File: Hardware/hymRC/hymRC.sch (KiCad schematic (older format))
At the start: 42 parts, among them U1 KT8870, U2 MCP23017_SP, Y1 3.5795M

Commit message: huda calisma
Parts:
- added R13: 1K, symbol Device:R
- added U4: OptoCoupler, Package_DIP:SMDIP-4_W9.53mm_Clearance8mm, symbol Isolator:SFH617A-1X007T
- added U5: LM358, symbol Amplifier_Operational:LM358
- added U6: 4001, Package_DIP:DIP-24_W16.51mm_SMDSocket_LongPads, symbol 4xxx:4001
- gave numbers to parts that had none: 33
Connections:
- wire segments 152 -> 158
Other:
- note added: "- SQELCH BILGISI Optocoupler'dan gecirilecek\n- DTMF girisi icin LM358 kullanilacak (huda)\n- Mors vb baglantisi yapilacak LM358 uzerinden\n- digital input 2 adet high 2 adet low trigger olacak\n- 1 role kanali daha eklenecek (2 kontak)\n- 5V icin LDO regulator ekle\n- Led uclari\n- link cihazindan gelen COR bilgisi alinirsa TX olacak, kuyruk olmayacak (lm358 i genislet)\n- link aktif ise bizim c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"

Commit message: audio buffers added
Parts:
- added C10, C11, C9: 100pF, symbol Device:C_Small
- added C12: 0.0068uF, symbol Device:C_Small
- added C13, C14, C8: 0.22uF, symbol Device:C_Small
- added C3, C4: 1uF, symbol Device:CP1
- added C5, C6, C7: 10uF, symbol Device:CP1
- added D5, D6: 1N914, Diode_THT:D_DO-35_SOD27_P7.62mm_Horizontal, symbol Diode:1N914
- added J?: RX RADIO, symbol Connector:Screw_Terminal_01x05
- added J?: TX RADIO, symbol Connector:Screw_Terminal_01x05
- added R22, R23: 1K3, symbol Device:R
- added R24: 91K, symbol Device:R
- added R25, R27: 100K, symbol Device:R
- added R26: 1M, symbol Device:R
- added R28, R29, R31: 12K, symbol Device:R
- added R30, R32, R33, R34, R35: 11K, symbol Device:R
- added RV1: 10K, symbol Device:R_POT
- added U7: TL084, symbol Amplifier_Operational:TL084
- added U8: LM7808_TO220, Package_TO_SOT_THT:TO-220-3_Vertical, symbol Regulator_Linear:LM7808_TO220
- added U9: L7805, symbol Regulator_Linear:L7805
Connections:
- net labels added: RX_AUDIO, RX_SQL, TX_AUDIO, TX_POWER, TX_PTT, VCC_2
- wire segments 158 -> 228
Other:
- note added: "? VCC/2 ??"
- note added: "REGULATORS"
- note added: "RX_TX RADIO TERMINALS"
- moved on the sheet: A1, D1, D2, D3, D4, J1, J2, J3, K1, K2, K3, K4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

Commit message: opkuplers added.. both negative and positive triggered
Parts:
- removed J1: Terminal, symbol Connector:Screw_Terminal_01x20
- removed J?: TX RADIO, symbol Connector:Screw_Terminal_01x05
- removed U5: LM358, symbol Amplifier_Operational:LM358
- removed U6: 4001, Package_DIP:DIP-24_W16.51mm_SMDSocket_LongPads, symbol 4xxx:4001
- added C15, C18, C23, C24, C29, C30: 0.22uF, symbol Device:C_Small
- added C16, C17, C25, C26, C27, C28: 100pF, symbol Device:C_Small
- added C19, C20, C21, C22, C31, C33, C34, C35, C36, C37: 0.1uF, symbol Device:C_Small
- added C32: 0.0068uF, symbol Device:C_Small
- added C38: 100nF, symbol Device:C_Small
- added C39: 10uF, symbol Device:CP1
- added D7: 1N4001, symbol Device:D
- added J1: Relay_0, symbol Connector:Screw_Terminal_01x03
- added J4: TX RADIO, symbol Connector:Screw_Terminal_01x06
- added J6: Relay_1, symbol Connector:Screw_Terminal_01x03
- added J7: Relay_2, symbol Connector:Screw_Terminal_01x03
- added J8: Relay_3, symbol Connector:Screw_Terminal_01x06
- added J9: Relay_4, symbol Connector:Screw_Terminal_01x06
- added K5: Role, Relay_THT:Relay_DPDT_FRT5, symbol Relay:AZ850P1-x
- added Q5: NPN, symbol Device:Q_NPN_EBC
- added R36, R50, R51: 1M, symbol Device:R
- added R37, R42, R48, R49, R52, R53, R62, R63: 100K, symbol Device:R
- added R38, R45, R54, R56: 10K, symbol Device:R
- added R39, R55, R57: 18K, symbol Device:R
- added R40, R41, R60, R61: 4K7, symbol Device:R
- added R43, R64, R65: 1M2, symbol Device:R
- added R44, R70: 1K, symbol Device:R
- added R46, R47: 91K, symbol Device:R
- added R58: 11K, symbol Device:R
- added R59: 12K, symbol Device:R
- added R66, R71, R75, R81, R85, R89, R90, R94, R95: 270, symbol Device:R
- added R67: 8K8, symbol Device:R
- added R68: 3K3, symbol Device:R
- added R69: 2K2, symbol Device:R
- added R72, R73, R74, R76, R77, R78, R79, R80, R82, R83, R84, R86, R87, R88: DNP, symbol Device:R
- added R91, R92, R93, R96, R97, R98: 0, symbol Device:R
- added RV2, RV3, RV4, RV5, RV6, RV7, RV8: 10K, symbol Device:R_POT
- added U10, U11, U12, U13, U5: OptoCoupler, Package_DIP:SMDIP-4_W9.53mm_Clearance8mm, symbol Isolator:SFH617A-1X007T
- added U6: TL084, symbol Amplifier_Operational:TL084
- C11: value 100pF -> 0.22uF
- C13, C14: value 0.22uF -> 0.1uF
- R12: value 1K -> 270
- R13: value 1K -> DNP
- R28: value 12K -> 10K
- R29: value 12K -> 18K
- R32: value 11K -> 91K
- R33, R34: value 11K -> 100K
- R35: value 11K -> 1M2
- gave numbers to parts that had none: 1
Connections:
- net labels added: CONTROL_OUTPUT_4, LINK_AUDIO_IN, LINK_AUDIO_OUT, LINK_PTT_CTRL, LINK_PTT_OUT, LINK_SQL, LINK_SQUELCH, MCU_MOD, PTT_CTRL, R4_COM1, R4_COM2, R4_NC1, R4_NC2, R4_NO1, R4_NO2
- net labels removed: GND2, PTT
- wire segments 228 -> 450
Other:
- note added: "AUDIO MIXER - BUFFERS"
- note added: "NEGATIVE\nR71 DNP\nR72 0\nR73 270\nR74 0DNP"
- note added: "NEGATIVE\nR90 DNP\nR91 0\nR92 0\nR93 DNP"
- note added: "POSITIVE\nR71 270\nR72 DNP\nR73 DNP\nR74 0"
- note added: "POSITIVE\nR90 270\nR91 DNP\nR92 DNP\nR93 0"
- note added: "PTT_CONTROL"
- note added: "RELAY CONTROLLED TERMINALS"
- note added: "YEDEK SES CIKIS"
- note added: "YEDEK SES GIRIS"
- note removed: "- SQELCH BILGISI Optocoupler'dan gecirilecek\n- DTMF girisi icin LM358 kullanilacak (huda)\n- Mors vb baglantisi yapilacak LM358 uzerinden\n- digital input 2 adet high 2 adet low trigger olacak\n- 1 role kanali daha eklenecek (2 kontak)\n- 5V icin LDO regulator ekle\n- Led uclari\n- link cihazindan gelen COR bilgisi alinirsa TX olacak, kuyruk olmayacak (lm358 i genislet)\n- link aktif ise bizim c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"
- note removed: "5V Regulator"
- note removed: "? VCC/2 ??"
- note removed: "DIGITAL INPUT OUTPUT TERMINAL"
- moved on the sheet: A1, C1, C10, C11, C12, C13, C14, C2, C3, C4, C5, C6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

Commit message: main component footprints and links added to library
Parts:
- U1: footprint Package_SO:SOIC-18W_7.5x11.6mm_P1.27mm -> Package_SO:SSOP-20_5.3x7.2mm_P0.65mm; bluemavi (none) -> https://bluemavi.com/vitrin/tablo_new.asp?adet=1&kitap_id=7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; digikey (none) -> https://www.digikey.com/en/products/detail/microchip-techno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; direnc.net (none) -> 18 bacaklisi var; fiyat (none) -> 8 TL
- U10, U11, U12, U13, U3, U4, U5: footprint Package_DIP:SMDIP-4_W9.53mm_Clearance8mm -> Package_DIP:SMDIP-4_W7.62mm; symbol Isolator:SFH617A-1X007T -> hymRC_components:SFH615A-3; bluemavi (none) -> https://bluemavi.com/vitrin/tablo_new.asp?adet=1&kitap_id=7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; digikey (none) -> https://www.digikey.com/en/products/detail/vishay-semicondu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; direnc.net (none) -> https://www.direnc.net/sfh615a-3x-smd-optokuplor; fiyat (none) -> 1TL
- U2: footprint Package_DIP:DIP-28_W7.62mm -> Package_SO:SOIC-28W_7.5x17.9mm_P1.27mm; DIRENC.NET (none) -> https://www.direnc.net/mcp23017e-so-soic-28-smd-io-expander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; bluemavi (none) -> -; digikey (none) -> https://www.digikey.com/en/products/detail/microchip-techno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; fiyat (none) -> 10TL
- U6, U7: footprint (none) -> Package_SO:SOIC-14_3.9x8.7mm_P1.27mm; symbol Amplifier_Operational:TL084 -> hymRC_components:TL084; bluemavi (none) -> https://bluemavi.com/vitrin/tablo_new.asp?adet=1&kitap_id=7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; digikey (none) -> https://www.digikey.com/en/products/detail/texas-instrument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; direnc.net (none) -> https://www.direnc.net/tl084-smd-jfet-input-operational-amp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; fiyat (none) -> 2TL
- U7: footprint (none) -> Package_SO:SOIC-14_3.9x8.7mm_P1.27mm; symbol Amplifier_Operational:TL084 -> hymRC_components:TL084; Direnc.net (none) -> https://www.direnc.net/tl084-smd-jfet-input-operational-amp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; Fiyat (yaklasik) (none) -> 2-3 TL; bluemavi (none) -> https://bluemavi.com/vitrin/tablo_new.asp?adet=1&kitap_id=7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; digikey (none) -> https://www.digikey.com/en/products/detail/texas-instrument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; direnc.net (none) -> https://www.direnc.net/tl084-smd-jfet-input-operational-amp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; fiyat (none) -> 2TL

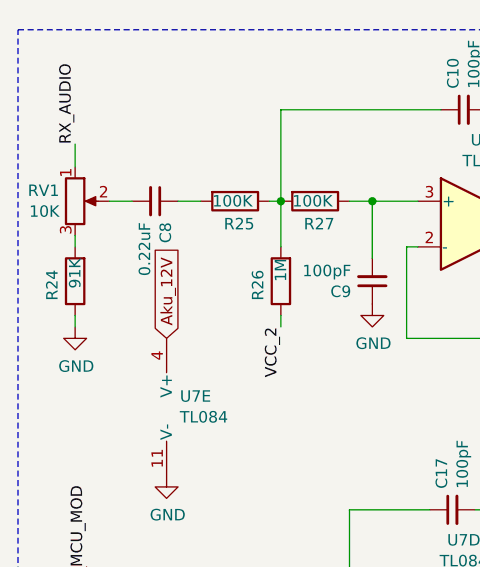
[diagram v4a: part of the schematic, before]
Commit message: resistors changed to smd 0805
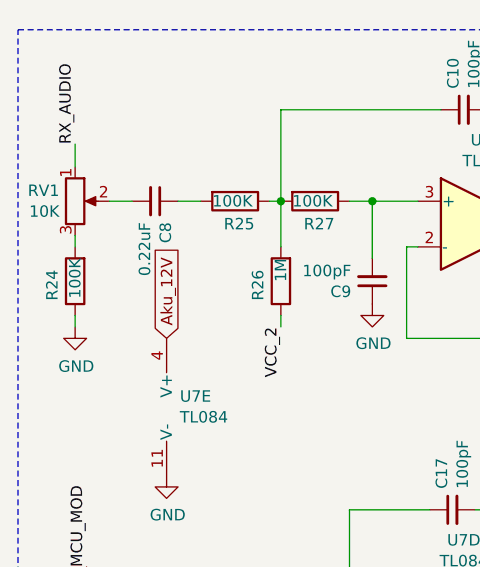
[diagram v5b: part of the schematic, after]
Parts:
- R1, R10, R11, R12, R13, R14, R15, R16, R17, R18, R19, R2, R20, R21, R22, R23, R25, R26, R27, R28, R29, R3, R30, R31, R33, R35, R4, R40, R41, R42, R43, R44, R45, R5, R6, R7, R71, R72, R73, R74, R75, R76, R77, R78, R79, R8, R80, R81, R82, R83, R84, R85, R86, R87, R88, R89, R9, R90, R91, R92, R93, R94, R95, R96, R97, R98: footprint (none) -> Resistor_SMD:R_0805_2012Metric_Pad1.20x1.40mm_HandSolder
- R24: value 91K -> 100K; footprint (none) -> Resistor_SMD:R_0805_2012Metric_Pad1.20x1.40mm_HandSolder

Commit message: test
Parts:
- added R100, R101, R102, R99: 27, Resistor_SMD:R_0805_2012Metric_Pad1.20x1.40mm_HandSolder, symbol Device:R
- R66, R67, R68, R69, R70: footprint (none) -> Resistor_SMD:R_0805_2012Metric_Pad1.20x1.40mm_HandSolder
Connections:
- net SPI_MISO: now also R101.1; no longer A1.15 (D12)
- net SPI_MOSI: now also R100.1; no longer A1.14 (D11)
- net SPI_SCK: now also R102.1; no longer A1.16 (D13)
- net SPI_SS: now also R99.1; no longer A1.13 (D10)
- new net: A1.13 (D10), R99.2
- new net: A1.14 (D11), R100.2
- new net: A1.15 (D12), R101.2
- new net: A1.16 (D13), R102.2
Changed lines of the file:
@@
 Text Notes 12850 3200 0    50   ~ 0
 MCU
-Text GLabel 11700 2650 0    50   Input ~ 0
+Text GLabel 11400 2650 0    50   Input ~ 0
 SPI_SCK
-Text GLabel 11700 2550 0    50   Input ~ 0
+Text GLabel 11400 2550 0    50   Input ~ 0
 SPI_MISO
-Text GLabel 11700 2450 0    50   Input ~ 0
+Text GLabel 11400 2450 0    50   Input ~ 0
 SPI_MOSI
-Text GLabel 11700 2350 0    50   Input ~ 0
+Text GLabel 11400 2350 0    50   Input ~ 0
 SPI_SS
 Text Label 11700 2150 2    50   ~ 0
@@
 F 0 "R67" V 11500 1900 50  0000 L CNN
 F 1 "8K8" V 11550 1650 50  0000 L CNN
-F 2 "" V 11480 1750 50  0001 C CNN
+F 2 "Resistor_SMD:R_0805_2012Metric_Pad1.20x1.40mm_HandSolder" V 11480 1750 50  0001 C CNN
 F 3 "~" H 11550 1750 50  0001 C CNN
 	1    11550 1750
@@
 F 0 "R68" V 11500 2000 50  0000 L CNN
 F 1 "3K3" V 11550 1750 50  0000 L CNN
-F 2 "" V 11480 1850 50  0001 C CNN
+F 2 "Resistor_SMD:R_0805_2012Metric_Pad1.20x1.40mm_HandSolder" V 11480 1850 50  0001 C CNN
 F 3 "~" H 11550 1850 50  0001 C CNN
 	1    11550 1850
@@
 F 0 "R69" V 11500 2100 50  0000 L CNN
 F 1 "2K2" V 11550 1850 50  0000 L CNN
-F 2 "" V 11480 1950 50  0001 C CNN
+F 2 "Resistor_SMD:R_0805_2012Metric_Pad1.20x1.40mm_HandSolder" V 11480 1950 50  0001 C CNN
 F 3 "~" H 11550 1950 50  0001 C CNN
 	1    11550 1950
@@
 F 0 "R70" V 11500 2200 50  0000 L CNN
 F 1 "1K" V 11550 1950 50  0000 L CNN
-F 2 "" V 11480 2050 50  0001 C CNN
+F 2 "Resistor_SMD:R_0805_2012Metric_Pad1.20x1.40mm_HandSolder" V 11480 2050 50  0001 C CNN
 F 3 "~" H 11550 2050 50  0001 C CNN
 	1    11550 2050
@@
 F 0 "R66" V 11200 2150 50  0000 L CNN
 F 1 "270" V 11100 2050 50  0000 L CNN
-F 2 "" V 11030 2150 50  0001 C CNN
+F 2 "Resistor_SMD:R_0805_2012Metric_Pad1.20x1.40mm_HandSolder" V 11030 2150 50  0001 C CNN
 F 3 "~" H 11100 2150 50  0001 C CNN
 	1    11100 2150
@@
 Wire Notes Line
 	550  7300 5050 7300
+$Comp
+L Device:R R99
+U 1 1 60628C97
+P 11550 2350
+F 0 "R99" V 11600 2450 50  0000 L CNN
+F 1 "27" V 11550 2250 50  0000 L CNN
+F 2 "Resistor_SMD:R_0805_2012Metric_Pad1.20x1.40mm_HandSolder" V 11480 2350 50  0001 C CNN
+F 3 "~" H 11550 2350 50  0001 C CNN
+	1    11550 2350
+	0    -1   -1   0
+$EndComp
+$Comp
+L Device:R R100
+U 1 1 606336F9
+P 11550 2450
+F 0 "R100" V 11600 2550 50  0000 L CNN
+F 1 "27" V 11550 2350 50  0000 L CNN
+F 2 "Resistor_SMD:R_0805_2012Metric_Pad1.20x1.40mm_HandSolder" V 11480 2450 50  0001 C CNN
+F 3 "~" H 11550 2450 50  0001 C CNN
+	1    11550 2450
+	0    -1   -1   0
+$EndComp
+$Comp
+L Device:R R101
+U 1 1 60633A99
+P 11550 2550
+F 0 "R101" V 11600 2650 50  0000 L CNN
+F 1 "27" V 11550 2450 50  0000 L CNN
+F 2 "Resistor_SMD:R_0805_2012Metric_Pad1.20x1.40mm_HandSolder" V 11480 2550 50  0001 C CNN
+F 3 "~" H 11550 2550 50  0001 C CNN
+	1    11550 2550
+	0    -1   -1   0
+$EndComp
+$Comp
+L Device:R R102
+U 1 1 60633E79
+P 11550 2650
+F 0 "R102" V 11600 2750 50  0000 L CNN
+F 1 "27" V 11550 2550 50  0000 L CNN
+F 2 "Resistor_SMD:R_0805_2012Metric_Pad1.20x1.40mm_HandSolder" V 11480 2650 50  0001 C CNN
+F 3 "~" H 11550 2650 50  0001 C CNN
+	1    11550 2650
+	0    -1   -1   0
+$EndComp
 $EndSCHEMATC

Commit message: capcsitors are 0805 now
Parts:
- added C40, C41, C45, C47: 10nF, Capacitor_SMD:C_0805_2012Metric_Pad1.18x1.45mm_HandSolder, symbol Device:C_Small
- added C42, C43, C44, C46: 100nF, Capacitor_SMD:C_0805_2012Metric_Pad1.18x1.45mm_HandSolder, symbol Device:C_Small
- C1, C10, C11, C12, C13, C14, C15, C16, C17, C18, C19, C2, C20, C21, C22, C23, C24, C25, C26, C27, C28, C29, C30, C31, C32, C33, C34, C35, C36, C37, C38, C8, C9: footprint (none) -> Capacitor_SMD:C_0805_2012Metric_Pad1.18x1.45mm_HandSolder
- C3, C39, C4, C5, C6, C7: footprint (none) -> Capacitor_SMD:CP_Elec_4x5.8
- D5, D6: footprint Diode_THT:D_DO-35_SOD27_P7.62mm_Horizontal -> Diode_SMD:D_0805_2012Metric_Pad1.15x1.40mm_HandSolder
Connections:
- net +5V: now also C44.2, C45.1, C46.2, C47.1
- net GND: now also C44.1, C45.2, C46.1, C47.2
- new net: C40.1, C43.2
- new net: C40.2, C43.1
- new net: C41.1, C42.2
- new net: C41.2, C42.1

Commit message: DRC checks resolved
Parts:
- added J10: EXT_AUD_IN, symbol Connector:Screw_Terminal_01x02
- added J11: EXT_AUD_OUT, symbol Connector:Screw_Terminal_01x02
- added R103, R104: 270, Resistor_SMD:R_0805_2012Metric_Pad1.20x1.40mm_HandSolder, symbol Device:R
- added R105, R106, R107: 0, Resistor_SMD:R_0805_2012Metric_Pad1.20x1.40mm_HandSolder, symbol Device:R
- added U14: OptoCoupler, Package_DIP:SMDIP-4_W7.62mm, symbol hymRC_components:SFH615A-3
- J1, J6, J7: footprint (none) -> TerminalBlock:TerminalBlock_bornier-3_P5.08mm
- J4, J8, J9: footprint (none) -> TerminalBlock:TerminalBlock_bornier-6_P5.08mm
- J5: footprint (none) -> TerminalBlock:TerminalBlock_bornier-5_P5.08mm
- K1, K2, K3: footprint Relay_THT:Relay_StandexMeder_DIP_LowProfile -> Relay_THT:Relay_SPDT_Finder_34.51_Vertical; symbol Relay:DIPxx-1Cxx-51x -> hymRC_components:Role-1; direnc.net (none) -> https://www.direnc.net/12v-ciklet-role-hk41f-12v-6a
- K4, K5: footprint Relay_THT:Relay_DPDT_FRT5 -> Relay_SMD:Relay_DPDT_Kemet_EE2_NUH; symbol Relay:AZ850P1-x -> hymRC_components:Role-2; bluemavi (none) -> https://bluemavi.com/vitrin/tablo_new.asp?adet=1&kitap_id=7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; direnc.net (none) -> https://www.direnc.net/tx2sa-2a-12vdc-1170ma-panasonic-role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; fiyat (none) -> 10TL
- Q1: value NPN -> BC817; footprint (none) -> Package_TO_SOT_SMD:SOT-23; symbol Device:Q_NPN_EBC -> hymRC_components:BC817; bluemavi (none) -> https://bluemavi.com/vitrin/tablo_new.asp?adet=1&kitap_id=7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; direnc.net (none) -> https://www.direnc.net/bc817-25-ht-npn-smd-transistor-sot-23; fiyat (none) -> 0.10TL
- Q2, Q3, Q4, Q5: footprint (none) -> Package_TO_SOT_SMD:SOT-23; symbol Device:Q_NPN_EBC -> hymRC_components:BC817; bluemavi (none) -> https://bluemavi.com/vitrin/tablo_new.asp?adet=1&kitap_id=7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; direnc.net (none) -> https://www.direnc.net/bc817-25-ht-npn-smd-transistor-sot-23; fiyat (none) -> 0.10TL
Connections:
- net Aku_12V is gone; now on net +12V: C3.1, R6.1, U6.4 (V+), U7.4 (V+), U8.1 (VI)
- net INTB is gone; now on net INTA: U2.20 (INTA)
- net Vin is gone; now on net VIN: A1.30 (VIN)
- net +12V: now also K1.A1, K2.A1, K3.A1; no longer K1.6, K2.6, K3.6
- net GND: now also Q1.2 (E), Q2.2 (E), Q3.2 (E), Q4.2 (E), Q5.2 (E), J10.1 (Pin_1), J11.2 (Pin_2), R103.1, R105.1; no longer Q1.1 (E), Q2.1 (E), Q3.1 (E), Q4.1 (E), Q5.1 (E)
- net INTA: no longer U2.19 (INTB)
- net R0_COM: now also K1.11; no longer K1.7
- net R0_NC: now also K1.12; no longer K1.1
- net R1_COM: now also K2.11; no longer K2.7
- net R1_NC: now also K2.12; no longer K2.1
- net R2_COM: now also K3.11; no longer K3.7
- net R2_NC: now also K3.12; no longer K3.1
- net R3_COM1: now also K4.4; no longer K4.3
- net R3_COM2: now also K4.9; no longer K4.8
- net R3_NC1: now also K4.3; no longer K4.2
- net R3_NC2: now also K4.10; no longer K4.9
- net R3_NO1: now also K4.5; no longer K4.4
- net R3_NO2: now also K4.8; no longer K4.7
- net R4_COM1: now also K5.4; no longer K5.3
- net R4_COM2: now also K5.9; no longer K5.8
- net R4_NC1: now also K5.3; no longer K5.2
- net R4_NC2: now also K5.10; no longer K5.9
- net R4_NO1: now also K5.5; no longer K5.4
- net R4_NO2: now also K5.8; no longer K5.7
- net TX_POWER: now also R106.2, R107.2
- net UART_RX: now also J3.7 (Pin_7)
- net UART_TX: now also J3.8 (Pin_8)
- net TX_PWR_CTRL: now reaches A1.25 (A6)
- net TX_PWR_CTRL: now also U14.1
- net at R4.1, R5.1: now also Q1.1 (B); no longer Q1.2 (B)
- net at D1.2 (A), Q1.3 (C): now also K1.A2; no longer K1.2
- net at D4.2 (A), Q4.3 (C): now also K4.12; no longer K4.10
- net at R8.1, R9.1: now also Q2.1 (B); no longer Q2.2 (B)
- net at D2.2 (A), Q2.3 (C): now also K2.A2; no longer K2.2
- net at R16.1, R17.1: now also Q3.1 (B); no longer Q3.2 (B)
- net at D3.2 (A), Q3.3 (C): now also K3.A2; no longer K3.2
- net at R20.1, R21.1: now also Q4.1 (B); no longer Q4.2 (B)
- net VIN: now reaches C4.1, C6.1, R22.1, U8.3 (VO), U9.1 (IN)
- net at C36.2: now also J11.1 (Pin_1)
- net at RV6.1: now also J10.2 (Pin_2)
- net at D7.2 (A), Q5.3 (C): now also K5.12; no longer K5.10
- net at R44.1, R45.1: now also Q5.1 (B); no longer Q5.2 (B)
- net +5V renamed 5V
- net 5V: now also R104.2; no longer A1.27 (+5V)
- new net: R103.2, U14.2
- new net: R105.2, R107.1, U14.3
- new net: R104.1, R106.1, U14.4
- no-connect marks 3 -> 9
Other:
- note added: "PTT / POWER CONTROL"
- note removed: "PTT_CONTROL"
- note removed: "YEDEK SES CIKIS"
- note removed: "YEDEK SES GIRIS"
- moved on the sheet: R94, R95, R96, R97, R98, U13
